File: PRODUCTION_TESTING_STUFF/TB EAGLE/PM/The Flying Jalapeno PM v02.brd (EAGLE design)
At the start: 85.1 x 91.4 mm, 10 parts

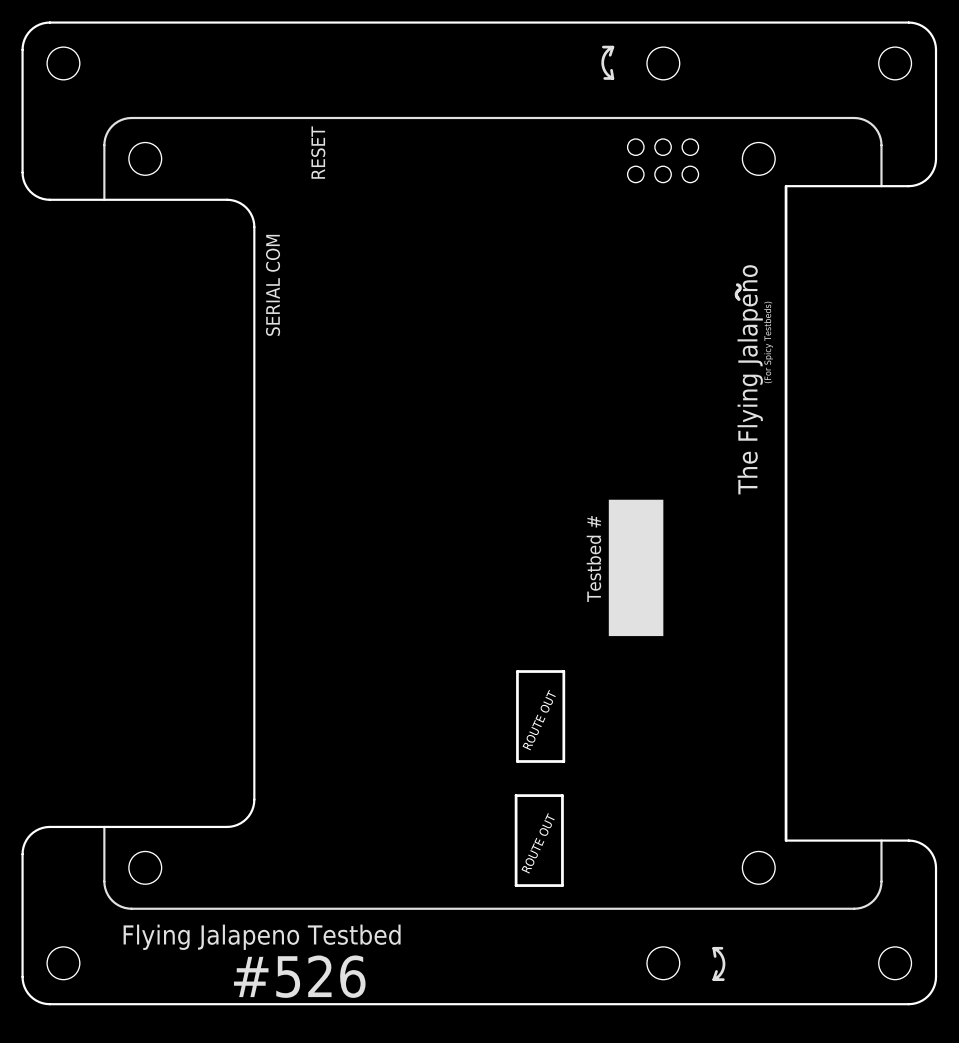
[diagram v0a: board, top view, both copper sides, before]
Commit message: Added cutouts in the PM to allow space for nylon standoffs
had to mill these out on v01. Originally planned on testing without
these populated.
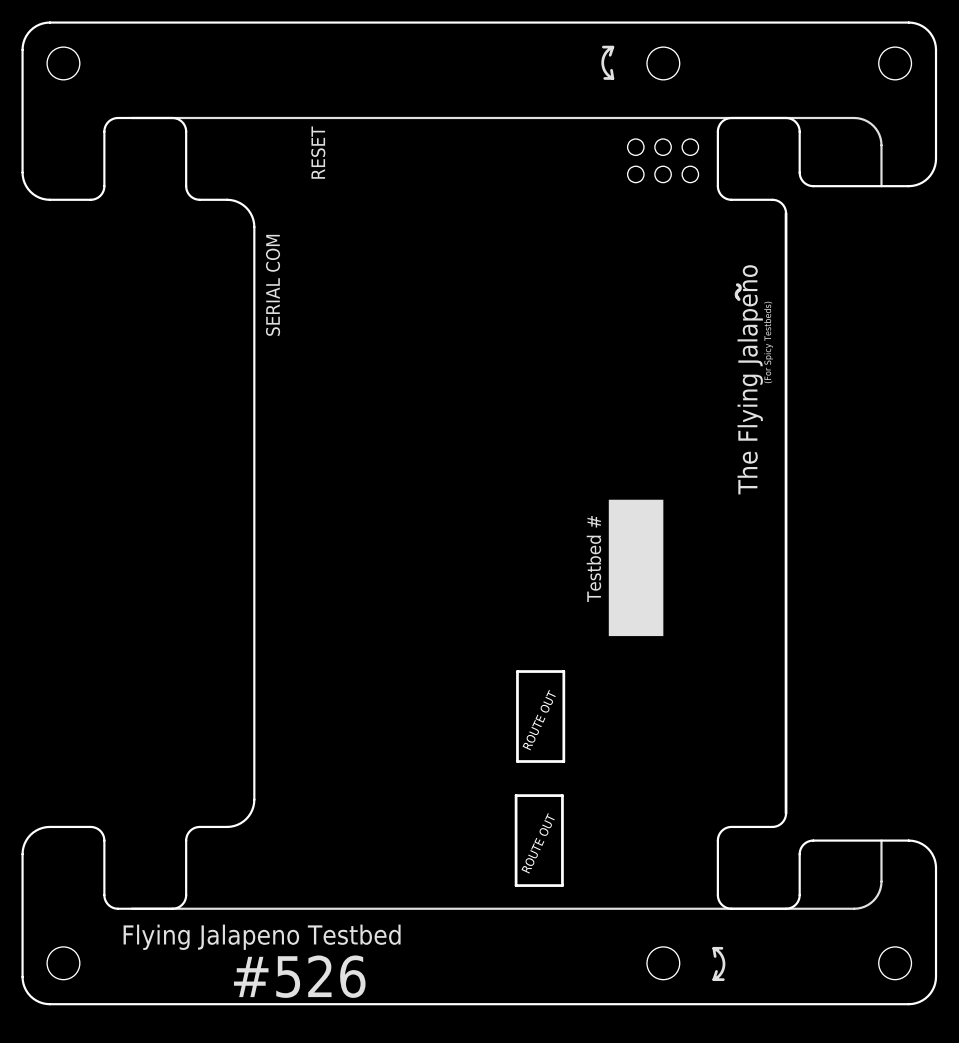
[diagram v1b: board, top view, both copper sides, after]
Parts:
- removed STANDOFF1, STANDOFF2, STANDOFF3, STANDOFF4: STAND-OFFTIGHT, SparkFun-Electromechanical:STAND-OFF-TIGHT
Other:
- outline, holes or cut-outs redrawn
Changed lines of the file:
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@@
 <?xml version="1.0" encoding="utf-8"?>
 <!DOCTYPE eagle SYSTEM "eagle.dtd">
-<eagle version="7.3.0">
+<eagle version="7.6.0">
 <drawing>
 <settings>
@@
 <setting verticaltext="up"/>
 </settings>
-<grid distance="0.05" unitdist="inch" unit="inch" style="lines" multiple="1" display="yes" altdistance="0.001" altunitdist="inch" altunit="inch"/>
+<grid distance="0.05" unitdist="inch" unit="inch" style="lines" multiple="1" display="yes" altdistance="0.005" altunitdist="inch" altunit="inch"/>
 <layers>
 <layer number="1" name="Top" color="4" fill="1" visible="yes" active="yes"/>
@@
 <layer number="47" name="Measures" color="7" fill="1" visible="no" active="yes"/>
 <layer number="48" name="Document" color="7" fill="1" visible="no" active="yes"/>
-<layer number="49" name="Reference" color="13" fill="1" visible="yes" active="yes"/>
+<layer number="49" name="Reference" color="13" fill="1" visible="no" active="yes"/>
 <layer number="50" name="dxf" color="7" fill="1" visible="no" active="yes"/>
 <layer number="51" name="tDocu" color="6" fill="1" visible="yes" active="yes"/>
@@
 <wire x1="46.101" y1="30.988" x2="46.101" y2="22.606" width="0.254" layer="20"/>
 <wire x1="80.01" y1="15.24" x2="71.12" y2="15.24" width="0.254" layer="49"/>
-<wire x1="71.12" y1="15.24" x2="71.12" y2="76.2" width="0.254" layer="20"/>
+<wire x1="71.12" y1="17.78" x2="71.12" y2="73.66" width="0.254" layer="20"/>
 <wire x1="71.12" y1="76.2" x2="80.01" y2="76.2" width="0.254" layer="49"/>
 <wire x1="2.54" y1="0" x2="0" y2="2.54" width="0.2032" layer="20" curve="-90"/>
@@
 <wire x1="2.54" y1="91.44" x2="0" y2="88.9" width="0.2032" layer="49" curve="90"/>
 <wire x1="0" y1="77.47" x2="2.54" y2="74.93" width="0.2032" layer="20" curve="90"/>
-<wire x1="2.54" y1="74.93" x2="19.05" y2="74.93" width="0.2032" layer="20"/>
+<wire x1="2.54" y1="74.93" x2="6.35" y2="74.93" width="0.2032" layer="20"/>
+<wire x1="16.51" y1="74.93" x2="19.05" y2="74.93" width="0.2032" layer="20"/>
 <wire x1="19.05" y1="74.93" x2="21.59" y2="72.39" width="0.2032" layer="20" curve="-90"/>
 <wire x1="21.59" y1="72.39" x2="21.59" y2="19.05" width="0.2032" layer="20"/>
 <wire x1="21.59" y1="19.05" x2="19.05" y2="16.51" width="0.2032" layer="20" curve="-90"/>
-<wire x1="19.05" y1="16.51" x2="2.54" y2="16.51" width="0.2032" layer="20"/>
+<wire x1="19.05" y1="16.51" x2="16.51" y2="16.51" width="0.2032" layer="20"/>
+<wire x1="6.35" y1="16.51" x2="2.54" y2="16.51" width="0.2032" layer="20"/>
 <wire x1="2.54" y1="16.51" x2="0" y2="13.97" width="0.2032" layer="20" curve="90"/>
 <wire x1="85.09" y1="78.74" x2="82.55" y2="76.2" width="0.2032" layer="20" curve="-90"/>
-<wire x1="82.55" y1="76.2" x2="71.12" y2="76.2" width="0.2032" layer="20"/>
-<wire x1="71.12" y1="15.24" x2="82.55" y2="15.24" width="0.2032" layer="20"/>
+<wire x1="82.55" y1="76.2" x2="73.66" y2="76.2" width="0.2032" layer="20"/>
+<wire x1="73.66" y1="15.24" x2="82.55" y2="15.24" width="0.2032" layer="20"/>
 <wire x1="82.55" y1="15.24" x2="85.09" y2="12.7" width="0.2032" layer="20" curve="-90"/>
 <wire x1="0" y1="13.97" x2="0" y2="2.54" width="0.2032" layer="20"/>
@@
 <text x="47.2724" y="23.5587875" size="0.8128" layer="20" font="vector" ratio="15" rot="R65">ROUTE OUT</text>
 <text x="47.17085" y="12.07821875" size="0.8128" layer="20" font="vector" ratio="15" rot="R65">ROUTE OUT</text>
-<wire x1="7.62" y1="74.93" x2="7.62" y2="80.01" width="0.2032" layer="21"/>
-<wire x1="7.62" y1="80.01" x2="10.16" y2="82.55" width="0.2032" layer="21" curve="-90"/>
 <wire x1="10.16" y1="82.55" x2="77.47" y2="82.55" width="0.2032" layer="21"/>
 <wire x1="77.47" y1="82.55" x2="80.01" y2="80.01" width="0.2032" layer="21" curve="-90"/>
@@
 <wire x1="80.01" y1="11.43" x2="77.47" y2="8.89" width="0.2032" layer="21" curve="-90"/>
 <wire x1="77.47" y1="8.89" x2="10.16" y2="8.89" width="0.2032" layer="21"/>
-<wire x1="10.16" y1="8.89" x2="7.62" y2="11.43" width="0.2032" layer="21" curve="-90"/>
-<wire x1="7.62" y1="11.43" x2="7.62" y2="16.51" width="0.2032" layer="21"/>
+<wire x1="73.66" y1="15.24" x2="72.39" y2="13.97" width="0.2032" layer="20" curve="90"/>
+<wire x1="72.39" y1="13.97" x2="72.39" y2="10.16" width="0.2032" layer="20"/>
+<wire x1="72.39" y1="10.16" x2="71.12" y2="8.89" width="0.2032" layer="20" curve="-90"/>
+<wire x1="71.12" y1="8.89" x2="66.04" y2="8.89" width="0.2032" layer="20"/>
+<wire x1="66.04" y1="8.89" x2="64.77" y2="10.16" width="0.2032" layer="20" curve="-90"/>
+<wire x1="64.77" y1="10.16" x2="64.77" y2="15.24" width="0.2032" layer="20"/>
+<wire x1="64.77" y1="15.24" x2="66.04" y2="16.51" width="0.2032" layer="20" curve="-90"/>
+<wire x1="66.04" y1="16.51" x2="69.85" y2="16.51" width="0.2032" layer="20"/>
+<wire x1="69.85" y1="16.51" x2="71.12" y2="17.78" width="0.2032" layer="20" curve="90"/>
+<wire x1="73.66" y1="76.2" x2="72.39" y2="77.47" width="0.2032" layer="20" curve="-90"/>
+<wire x1="72.39" y1="77.47" x2="72.39" y2="81.28" width="0.2032" layer="20"/>
+<wire x1="72.39" y1="81.28" x2="71.12" y2="82.55" width="0.2032" layer="20" curve="90"/>
+<wire x1="71.12" y1="82.55" x2="66.04" y2="82.55" width="0.2032" layer="20"/>
+<wire x1="66.04" y1="82.55" x2="64.77" y2="81.28" width="0.2032" layer="20" curve="90"/>
+<wire x1="64.77" y1="81.28" x2="64.77" y2="76.2" width="0.2032" layer="20"/>
+<wire x1="64.77" y1="76.2" x2="66.04" y2="74.93" width="0.2032" layer="20" curve="90"/>
+<wire x1="66.04" y1="74.93" x2="69.85" y2="74.93" width="0.2032" layer="20"/>
+<wire x1="69.85" y1="74.93" x2="71.12" y2="73.66" width="0.2032" layer="20" curve="-90"/>
+<wire x1="16.51" y1="74.93" x2="15.24" y2="76.2" width="0.2032" layer="20" curve="-90"/>
+<wire x1="15.24" y1="76.2" x2="15.24" y2="81.28" width="0.2032" layer="20"/>
+<wire x1="15.24" y1="81.28" x2="13.97" y2="82.55" width="0.2032" layer="20" curve="90"/>
+<wire x1="13.97" y1="82.55" x2="8.89" y2="82.55" width="0.2032" layer="20"/>
+<wire x1="8.89" y1="82.55" x2="7.62" y2="81.28" width="0.2032" layer="20" curve="90"/>
+<wire x1="7.62" y1="81.28" x2="7.62" y2="76.2" width="0.2032" layer="20"/>
+<wire x1="7.62" y1="76.2" x2="6.35" y2="74.93" width="0.2032" layer="20" curve="-90"/>
+<wire x1="16.51" y1="16.51" x2="15.24" y2="15.24" width="0.2032" layer="20" curve="90"/>
+<wire x1="15.24" y1="15.24" x2="15.24" y2="10.16" width="0.2032" layer="20"/>
+<wire x1="15.24" y1="10.16" x2="13.97" y2="8.89" width="0.2032" layer="20" curve="-90"/>
+<wire x1="13.97" y1="8.89" x2="8.89" y2="8.89" width="0.2032" layer="20"/>
+<wire x1="8.89" y1="8.89" x2="7.62" y2="10.16" width="0.2032" layer="20" curve="-90"/>
+<wire x1="7.62" y1="10.16" x2="7.62" y2="15.24" width="0.2032" layer="20"/>
+<wire x1="7.62" y1="15.24" x2="6.35" y2="16.51" width="0.2032" layer="20" curve="90"/>
 </plain>
 <attributes>
@@
 </autorouter>
 <elements>
-<element name="STANDOFF1" library="SparkFun-Electromechanical" package="STAND-OFF-TIGHT" value="STAND-OFFTIGHT" x="68.58" y="12.7" rot="R90"/>
-<element name="STANDOFF2" library="SparkFun-Electromechanical" package="STAND-OFF-TIGHT" value="STAND-OFFTIGHT" x="68.58" y="78.74" rot="R90"/>
-<element name="STANDOFF3" library="SparkFun-Electromechanical" package="STAND-OFF-TIGHT" value="STAND-OFFTIGHT" x="11.43" y="78.74" rot="R90"/>
-<element name="STANDOFF4" library="SparkFun-Electromechanical" package="STAND-OFF-TIGHT" value="STAND-OFFTIGHT" x="11.43" y="12.7" rot="R90"/>
 <element name="STANDOFF5" library="SparkFun-Electromechanical" package="STAND-OFF-TIGHT" value="STAND-OFFTIGHT" x="81.28" y="3.81"/>
 <element name="STANDOFF6" library="SparkFun-Electromechanical" package="STAND-OFF-TIGHT" value="STAND-OFFTIGHT" x="3.81" y="3.81"/>
